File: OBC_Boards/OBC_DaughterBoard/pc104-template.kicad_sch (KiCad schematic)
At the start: 35 parts, among them J1 PC104_Connector, J2 ST11S008V4HR2000, U1 MCP79400T-I/SN, U2 MCP7940NT-I_MS, U3 BU33SA5WGWZ-E2-qsat-symb, Y1 CM9V-T1A

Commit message: working on pinout
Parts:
- removed G1: CR2032H, CR2032H:CR2032H, symbol CR2032H:CR2032H
- removed R?: 33, Daughterboard_footprints:RESC1608X55N, symbol Device:R
- removed R?: 10k, Daughterboard_footprints:RESC1608X55N, symbol Device:R
- added BT?: BVSD-2032-PC, Daughterboard_footprints:BAT_BVSD-2032-PC, symbol Daughterboard_Symbols:BVSD-2032-PC
- added C? (x2): 18pF, CAPC1608X90N, symbol Daughterboard_Symbols:CL10B104KB8NNNL
- added C? (x2): 10uF, CAPC1608X90N, symbol Daughterboard_Symbols:CL10B104KB8NNNL
- added C?: 0.1uF, CAPC1608X90N, symbol Daughterboard_Symbols:CL10B104KB8NNNL
- added FB? (x2): 100R @ 100 MHz, Daughterboard_footprints:BEADC1608X75N, symbol Device:FerriteBead_Small
- added J? (x3): Conn_01x04, Connector_PinHeader_2.54mm:PinHeader_1x04_P2.54mm_Vertical, symbol Connector_Generic:Conn_01x04
- added J?: Conn_02x06_Odd_Even, Connector_PinHeader_2.54mm:PinHeader_2x06_P2.54mm_Horizontal, symbol Connector_Generic:Conn_02x06_Odd_Even
- added R?: 33, Daughterboard_footprints:RESC1608X55N, symbol Device:R
- added R?: 20k, Daughterboard_footprints:RESC1608X55N, symbol Device:R
- added TP?: TestPoint, symbol Connector:TestPoint
- added U?: JS102011SCQN, Daughterboard_footprints:JS102011SCQN, symbol Daughterboard_Symbols:JS102011SCQN
- U3: footprint (none) -> STM32_Breakout:BU33SA5WGWZ-E2
- gave numbers to parts that had none: 17
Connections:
- net I2C_SCL is gone; now on net I2C_SCL1: U2.2 (X2)
- net I2C_SDA is gone; now on net I2C_SDA1: U2.1 (X1)
- net out is gone; now on net +3V3: MAX4372F1.6 (RS-), R1.2
- net +3.3V: now also C?.2
- net +3V3: now also J3.1 (Pin_1), J3.17 (Pin_17), FB?.1, FB?.2, TP?.1
- net GND: now also J1.81 (H2-29), J2.11 (GND1), J2.12 (GND2), J2.13 (GND3), J2.14 (GND4), J2.15 (GND5), J2.16 (GND6), J2.17 (GND7), J2.6 (VSS), J3.14 (Pin_14), J3.20 (Pin_20), J3.25 (Pin_25), J3.30 (Pin_30), J3.34 (Pin_34), J3.39 (Pin_39), J3.6 (Pin_6), J3.7 (Pin_7), J4.2 (Pin_2), J5.2 (Pin_2), C?.1, C?.1, C?.1, C?.2, C?.2, J?.2 (Pin_2), J?.2 (Pin_2), J?.2 (Pin_2), J?.3 (Pin_3), J?.4 (Pin_4)
- net GPIO_pin: now also R8.2, R?.2
- net PM_Input: now also J4.1 (Pin_1), MAX4372F1.8 (RS+), R1.1
- net at U1.1 (X1), Y1.1: now also C?.2
- net at U1.2 (X2), Y1.2: now also C?.2
- net UART_RXD0: now reaches J3.10 (Pin_10)
- net I2C_SDA6: now reaches J3.15 (Pin_15)
- net I2C_SCL6: now reaches J3.16 (Pin_16)
- net SPI1_MOSI: now reaches J3.19 (Pin_19)
- net SPI1_MOSI: now also J2.3 (CMD/DI)
- net 5V_Rpi_Input: now reaches J3.2 (Pin_2)
- net 5V_Rpi_Input: now also J3.4 (Pin_4), J5.1 (Pin_1), U4.2
- net SPI1_MISO: now reaches J3.21 (Pin_21)
- net SPI1_MISO: now also J2.7 (DAT0/DO)
- net SPI1_CLK: now reaches J3.23 (Pin_23)
- net SPI1_CLK: now also J2.5 (CLK)
- net SPI1_CE0_N: now reaches J3.24 (Pin_24)
- net SPI1_CE0_N: now also J2.2 (CS/DAT3)
- net SPI1_CE1_N: now reaches J3.26 (Pin_26)
- net I2C_SDA1: now reaches J3.3 (Pin_3)
- net I2C_SDA1: now also R4.2, U1.5 (SDA), J?.4 (Pin_4), J?.4 (Pin_4), J?.4 (Pin_4), J?.6 (Pin_6)
- net I2C_SDA5: now reaches J3.32 (Pin_32)
- net SPI_SCL5: now reaches J3.33 (Pin_33)
- net GPIO16: now reaches J3.36 (Pin_36)
- net GPIO16: now also J?.8 (Pin_8)
- net GPIO26: now reaches J3.37 (Pin_37)
- net GPIO26: now also J?.9 (Pin_9)
- net GPIO20: now reaches J3.38 (Pin_38)
- net GPIO20: now also J?.7 (Pin_7)
- net GPIO21: now reaches J3.40 (Pin_40)
- net GPIO21: now also J?.10 (Pin_10)
- net I2C_SCL1: now reaches J3.5 (Pin_5)
- net I2C_SCL1: now also R3.2, U1.6 (SCL), J?.3 (Pin_3), J?.3 (Pin_3), J?.3 (Pin_3), J?.5 (Pin_5)
- net UART_TXD0: now reaches J3.8 (Pin_8)
- net at J2.4 (VDD): now also R?.2
- net 5V_SInput: now reaches U4.3
- net 5V_SInput: now also U?.2
- net at C2.1, U3.2 (Output): now also R?.1; no longer R8.2
- net 5V_BInput: now reaches J1.77 (H2-25)
- net 5V_BInput: now also U?.3
- removed net +5V: MAX4372F1.1 (VCC), MAX4372F1.8 (RS+), R1.1
- net 5V_Input renamed 5V_VC_Input
- new net: R2.2, U1.7 (MFP)
- new net: FB?.1, MAX4372F1.1 (VCC)
- new net: C?.1, C?.1, FB?.2, R?.1
- new net 3V3_Input: J?.1 (Pin_1), J?.1 (Pin_1), J?.1 (Pin_1)
- new net 3V3_Output: J?.1 (Pin_1)
- new net 5V_CHG: J?.12 (Pin_12)
- new net 5V_DInput: J?.2 (Pin_2), U?.1
- new net GND_CHG: J?.11 (Pin_11)
- no-connect marks 106 -> 107
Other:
- moved on the sheet: J2, J3, J4, J5, U4

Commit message: Added MCP3008 to convert current monitor analog to serial for pi
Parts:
- added U5: MCP3008, MCP3008:Microchip-MCP3008-I_P-Manufacturer_Recommended, symbol Analog_ADC:MCP3008
- gave numbers to parts that had none: 16
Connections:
- net +3V3: now also MAX4372F1.5 (NC), U5.15 (Vref), U5.16 (Vdd)
- net GND: now also U5.14 (AGND), U5.9 (DGND); no longer MAX4372F1.3 (GND)
- net PM_Input: no longer MAX4372F1.8 (RS+), R1.1
- net SPI1_CLK: now also U5.13 (CLK)
- net SPI1_MISO: now also U5.12 (Dout)
- net SPI1_MOSI: now also U5.11 (Din)
- net at MAX4372F1.4 (OUT): now also U5.1 (CH0)
- new net: MAX4372F1.8 (RS+), R1.1
- new net GPIO_22?: U5.10 (~{CS}/SHDN)
- no-connect marks 107 -> 106
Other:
- note removed: "Current monitor"
- moved on the sheet: FB3, MAX4372F1, R1, TP1

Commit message: updates to schematic
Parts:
- removed J9: Conn_01x04, Connector_PinHeader_2.54mm:PinHeader_1x04_P2.54mm_Vertical, symbol Connector_Generic:Conn_01x04
- removed U4, U6: JS102011SCQN, Daughterboard_footprints:JS102011SCQN, symbol Daughterboard_Symbols:JS102011SCQN
- added D? (x2): RED, Daughterboard_footprints:CAPC1608X90N, symbol Simulation_SPICE:DIODE
- added FB? (x2): 100R @ 100 MHz, Daughterboard_footprints:BEADC1608X75N, symbol Device:FerriteBead_Small
- added J? (x2): Conn_01x04, Connector_PinHeader_2.54mm:PinHeader_1x04_P2.54mm_Vertical, symbol Connector_Generic:Conn_01x04
- added R? (x2): 2.2k, Daughterboard_footprints:RESC1608X55N, symbol Device:R
- added S1: EG1218, Daughterboard_footprints:EG1218, symbol Daughterboard_Symbols:EG1218
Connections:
- net 5V_CHG is gone; now on net BatVBUS: J6.12 (Pin_12)
- net 5V_DInput is gone; now on net 5V_Debug_Input: J6.2 (Pin_2)
- net 5V_VC_Input is gone; now on net 5V_Rpi_Input: FB1.2
- net GPIO_pin is gone; now on net Analog_Voltage: R7.2, R8.2
- net I2C_SCL6 is gone; now on net UART_RTS: J3.16 (Pin_16)
- net I2C_SDA6 is gone; now on net UART_CTS: J3.15 (Pin_15)
- net +3.3V: now also FB?.1; no longer C6.2, U1.8 (VCC)
- net +3V3: no longer J3.1 (Pin_1)
- net 3V3_Input: now also J?.1 (Pin_1), J?.1 (Pin_1)
- net 5V_Rpi_Input: now also S1.S
- net GND: now also J1.99 (H2-47), MAX4372F1.3 (GND), J?.2 (Pin_2), J?.2 (Pin_2), R?.2, R?.2; no longer J1.81 (H2-29)
- net I2C_SCL1: now also J1.10 (H1-10), J1.12 (H1-12), J1.14 (H1-14), J1.45 (H1-45), J1.6 (H1-6), J1.8 (H1-8)
- net I2C_SDA1: now also J1.11 (H1-11), J1.13 (H1-13), J1.44 (H1-44), J1.5 (H1-5), J1.7 (H1-7), J1.9 (H1-9)
- net UART_RXD0: now also J1.2 (H1-2)
- net UART_TXD0: now also J1.1 (H1-1)
- net GPIO6: now reaches J3.31 (Pin_31)
- net GPIO6: now also J?.3 (Pin_3)
- net GPIO19: now reaches J3.35 (Pin_35)
- net GPIO19: now also J?.4 (Pin_4)
- net at C7.1, C8.1, FB4.2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: now also D?.1 (A)
- net 3V3: now reaches MAX4372F1.8 (RS+), R1.1
- net 3V3: now also J3.1 (Pin_1), J4.1 (Pin_1), FB?.1
- net Analog_Voltage: now reaches U5.2 (CH1)
- net UART_CTS: now reaches J1.3 (H1-3)
- net UART_RTS: now reaches J1.4 (H1-4)
- net 5V_Debug_Input: now reaches J1.68 (H1-16)
- net 5V_Debug_Input: now also S1.P
- net BatVBUS: now reaches J1.97 (H2-45)
- net 5V_BInput: no longer names the net of J1.77 (H2-25)
- net GPIO_22? renamed SPI1_CEO_N
- net I2C_SDA5 renamed GPIO12
- net GPIO12: now also J?.4 (Pin_4)
- net PM_Input: no longer names the net of U3.4 (Vout)
- net PM_Input: now also FB?.2; no longer J4.1 (Pin_1)
- net SPI_SCL5 renamed GPIO13
- net GPIO13: now also J?.3 (Pin_3)
- new net: C6.2, D?.1 (A), FB?.2, U1.8 (VCC)
- new net: D?.2 (K), R?.1 (x2)
- no-connect marks 106 -> 88
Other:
- moved on the sheet: C6, J4, J5, J6, J7, J8, TP1

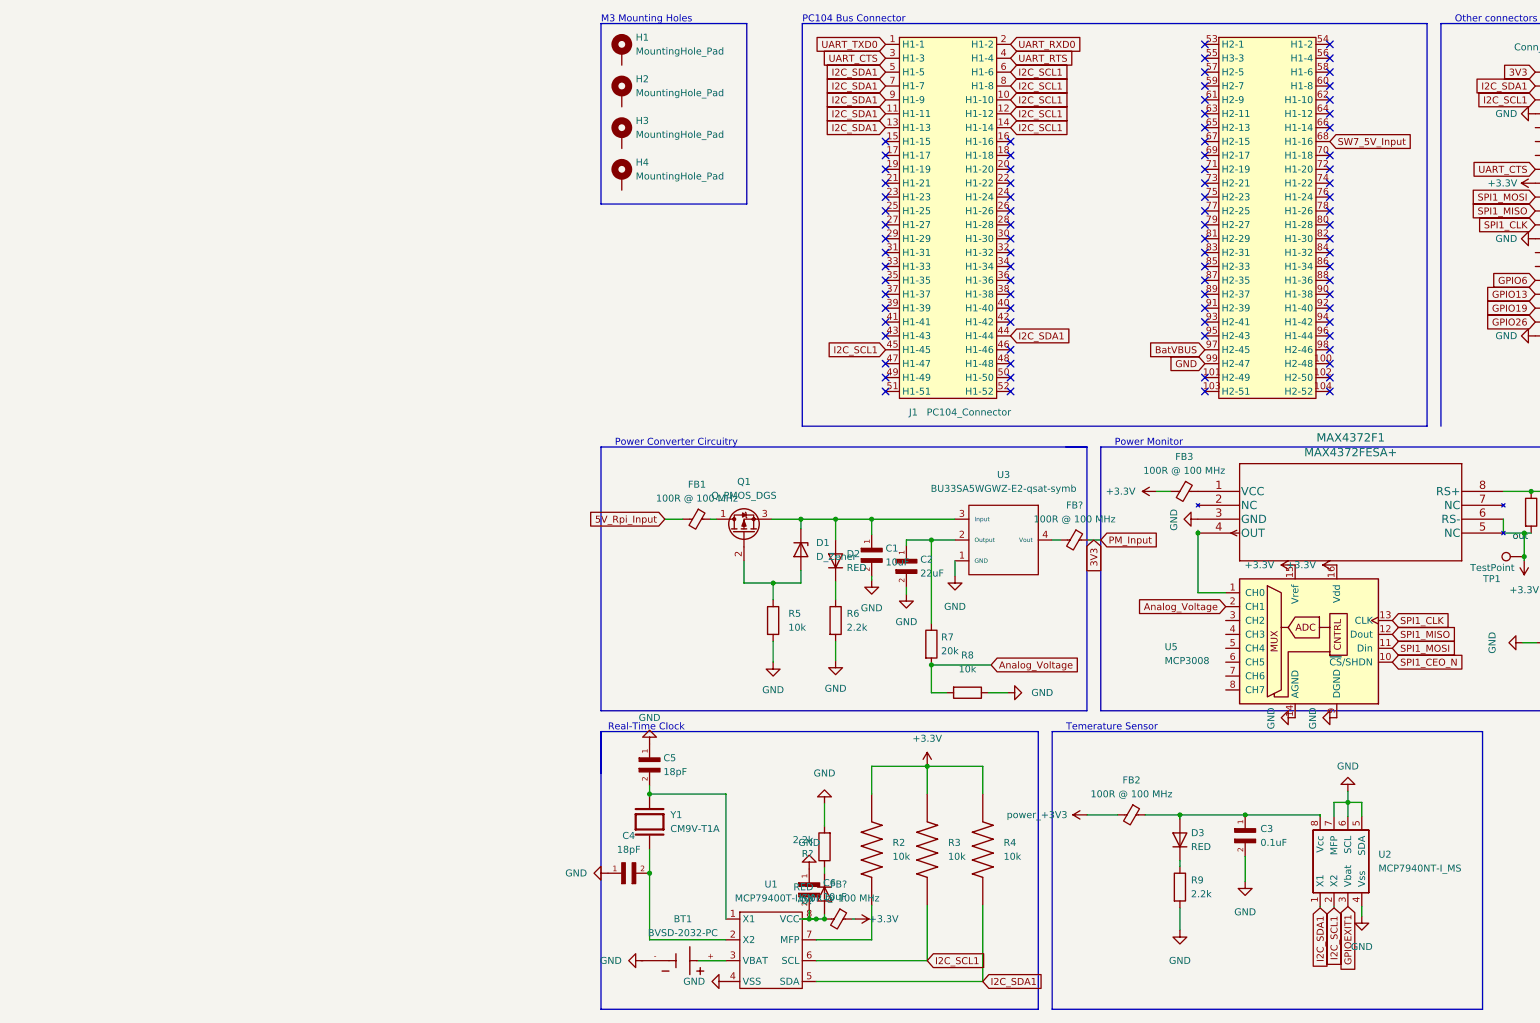
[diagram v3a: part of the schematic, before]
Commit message: obc: daughterboard: redo signal flags on pc104 bus connector
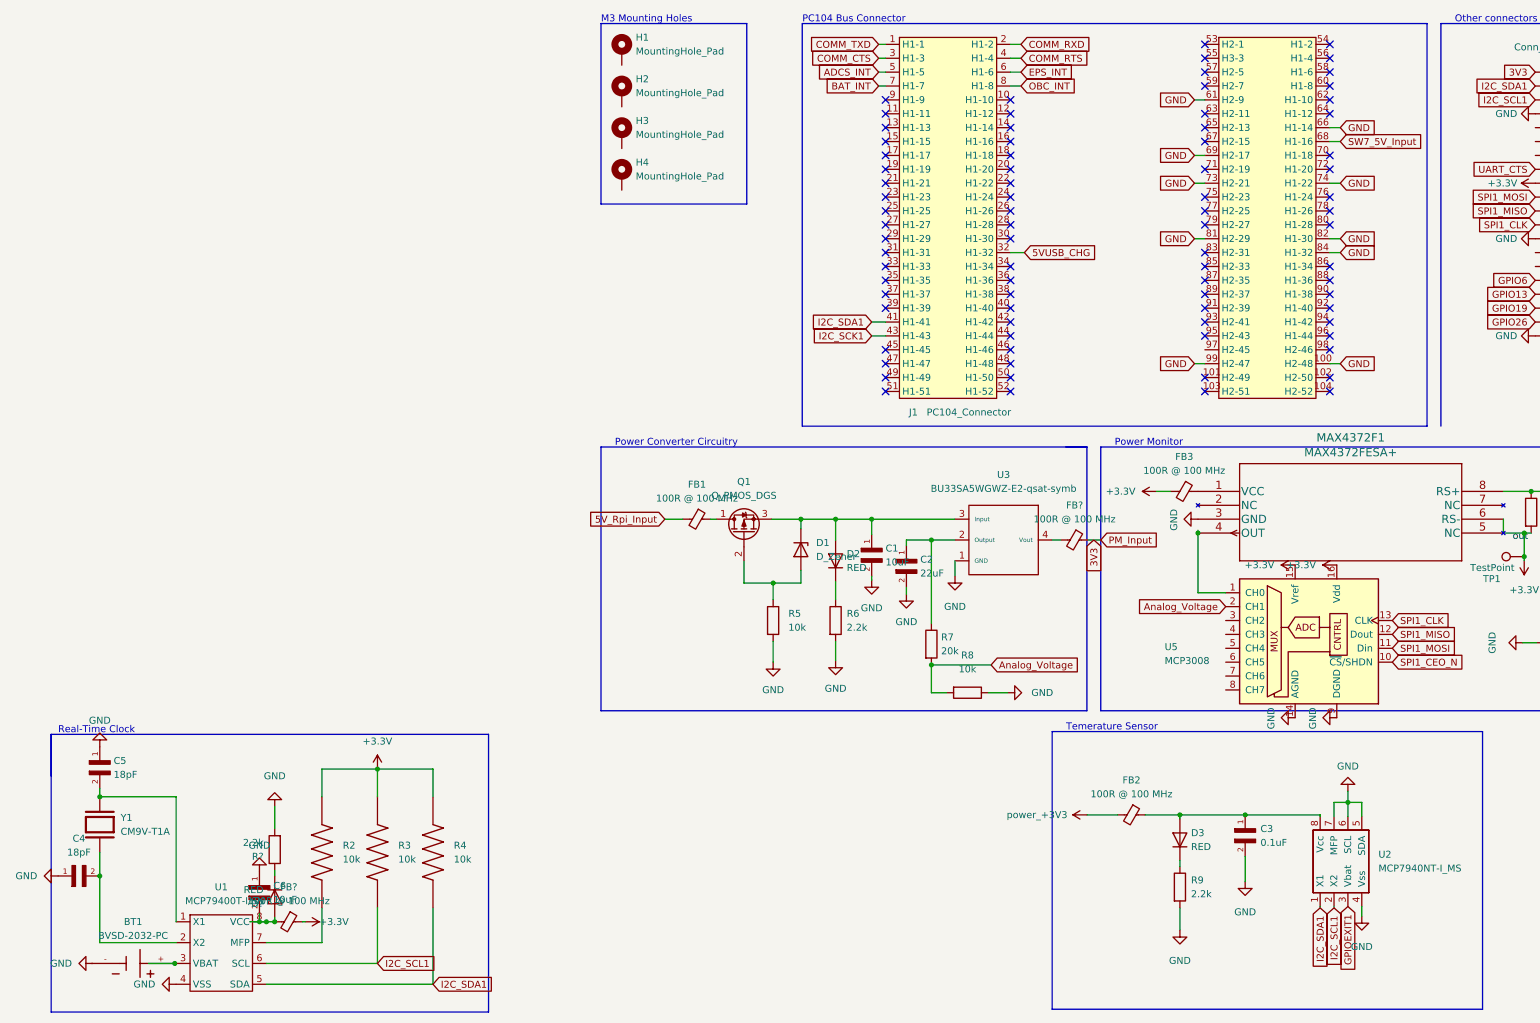
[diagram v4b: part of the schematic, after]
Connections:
- net BatVBUS: no longer J1.97 (H2-45)
- net GND: now also J1.100 (H2-48), J1.61 (H2-9), J1.66 (H1-14), J1.69 (H2-17), J1.73 (H2-21), J1.74 (H1-22), J1.81 (H2-29), J1.82 (H1-30), J1.84 (H1-32)
- net I2C_SCL1: no longer J1.10 (H1-10), J1.12 (H1-12), J1.14 (H1-14), J1.45 (H1-45), J1.6 (H1-6), J1.8 (H1-8)
- net I2C_SDA1: now also J1.41 (H1-41); no longer J1.11 (H1-11), J1.13 (H1-13), J1.44 (H1-44), J1.5 (H1-5), J1.7 (H1-7), J1.9 (H1-9)
- net UART_CTS: no longer J1.3 (H1-3)
- net UART_RTS: no longer J1.4 (H1-4)
- net UART_RXD0: no longer J1.2 (H1-2)
- net UART_TXD0: no longer J1.1 (H1-1)
- net at U1.3 (VBAT): now also BT1.+
- net 5VUSB_CHG: now reaches J1.32 (H1-32)
- net I2C_SCK1: now reaches J1.43 (H1-43)
- new net ADCS_INT: J1.5 (H1-5)
- new net BAT_INT: J1.7 (H1-7)
- new net COMM_CTS: J1.3 (H1-3)
- new net COMM_RTS: J1.4 (H1-4)
- new net COMM_RXD: J1.2 (H1-2)
- new net COMM_TXD: J1.1 (H1-1)
- new net EPS_INT: J1.6 (H1-6)
- new net OBC_INT: J1.8 (H1-8)
- no-connect marks 88 -> 84
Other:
- moved on the sheet: BT1, C4, C5, C6, D?, FB?, R2, R3, R4, R?, U1, Y1

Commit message: obc: daughterboard: clean up rtc section using hierarchical sheet
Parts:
- removed BT1: BVSD-2032-PC, Daughterboard_footprints:BAT_BVSD-2032-PC, symbol Daughterboard_Symbols:BVSD-2032-PC
- removed C4, C5: 18pF, CAPC1608X90N, symbol Daughterboard_Symbols:CL10B104KB8NNNL
- removed C6: 10uF, CAPC1608X90N, symbol Daughterboard_Symbols:CL10B104KB8NNNL
- removed D?: RED, Daughterboard_footprints:CAPC1608X90N, symbol Simulation_SPICE:DIODE
- removed FB?: 100R @ 100 MHz, Daughterboard_footprints:BEADC1608X75N, symbol Device:FerriteBead_Small
- removed R2, R3, R4: 10k, RESC1608X55N, symbol ESR03EZPF1002:ESR03EZPF1002
- removed R?: 2.2k, Daughterboard_footprints:RESC1608X55N, symbol Device:R
- removed U1: MCP79400T-I/SN, RTC Footprint:SOIC127P600X175-8N, symbol Timer_RTC:MCP79400T-I/SN
- removed Y1: CM9V-T1A, CM9V-T1A-32:XTAL_CM9V-T1A-32.768KHZ-9PF-20PPM-TA-QC, symbol CM9V-T1A-32.768KHZ-9PF-20PPM-TA-QC:CM9V-T1A-32.768KHZ-9PF-20PPM-TA-QC
- added R? (x3): 10k, RESC1608X55N, symbol ESR03EZPF1002:ESR03EZPF1002
- gave numbers to parts that had none: 5
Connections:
- net +3.3V: now also R?.1, R?.1, R?.1
- net I2C_SCK1: now also R?.2
- net I2C_SDA1: now also R?.2
- new net RTC_MFP: R?.2
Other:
- added sheet Real Time Clock (real-time-clock.kicad_sch)
- note added: "Pull Up Resistors"
- note removed: "Real-Time Clock"

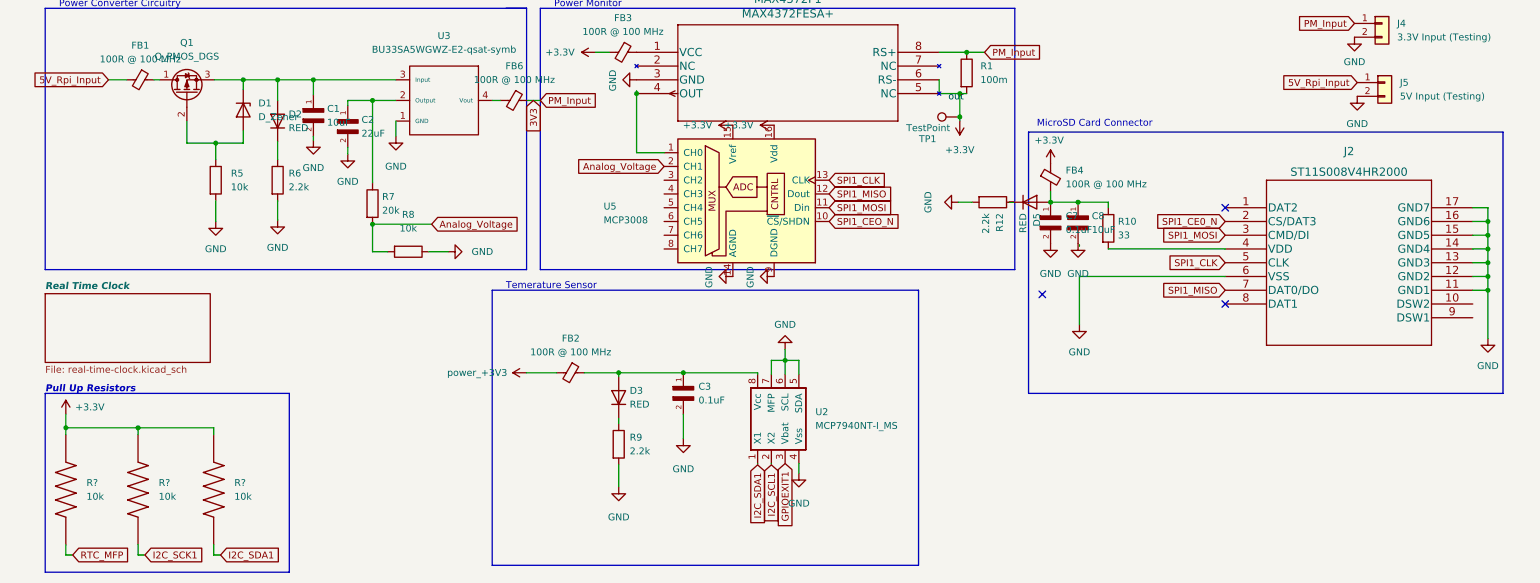
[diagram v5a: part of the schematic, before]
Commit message: obc: daughterboard: clean up microsd card section using hierarchical sheet
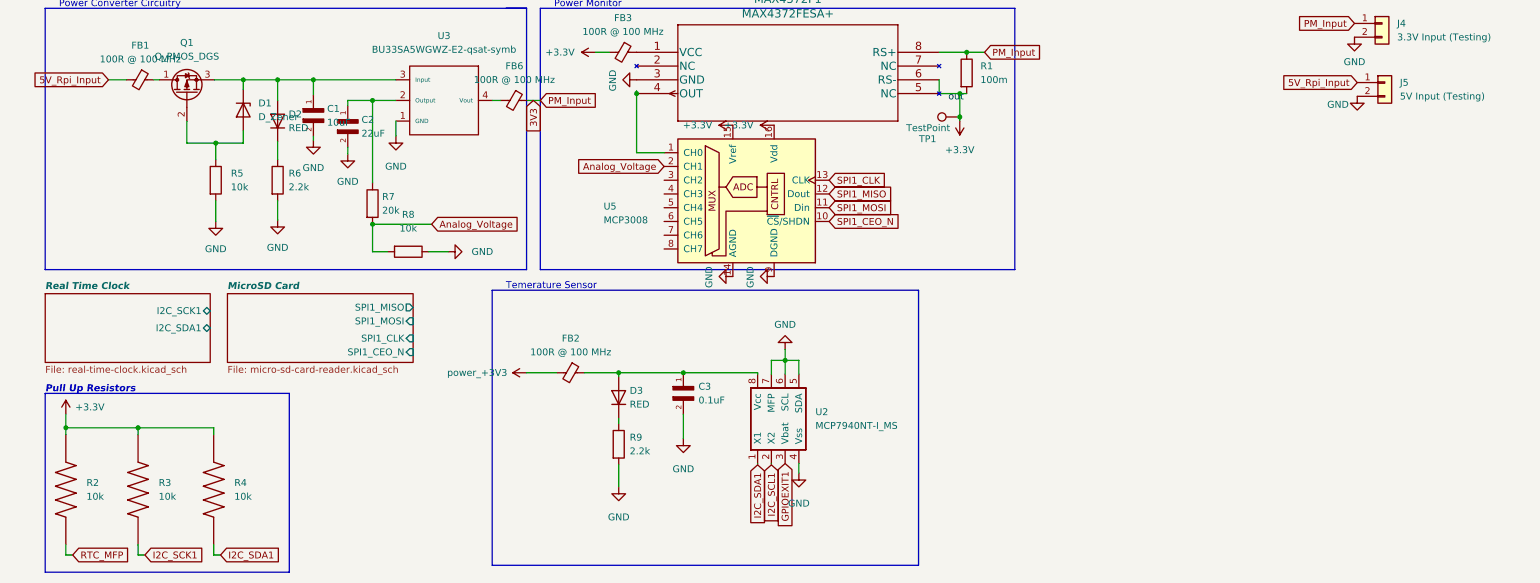
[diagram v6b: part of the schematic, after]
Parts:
- removed C7: 0.1uF, CAPC1608X90N, symbol Daughterboard_Symbols:CL10B104KB8NNNL
- removed C8: 10uF, CAPC1608X90N, symbol Daughterboard_Symbols:CL10B104KB8NNNL
- removed D5: RED, Daughterboard_footprints:CAPC1608X90N, symbol Simulation_SPICE:DIODE
- removed FB4: 100R @ 100 MHz, Daughterboard_footprints:BEADC1608X75N, symbol Device:FerriteBead_Small
- removed J2: ST11S008V4HR2000, STM32_Breakout:ST11S008V4HR2000, symbol Buffer:ST11S008V4HR2000
- removed R10: 33, Daughterboard_footprints:RESC1608X55N, symbol Device:R
- removed R12: 2.2k, Daughterboard_footprints:RESC1608X55N, symbol Device:R
- gave numbers to parts that had none: 3
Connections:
- no-connect marks 84 -> 81
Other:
- added sheet MicroSD Card (micro-sd-card-reader.kicad_sch)
- sheet Real Time Clock ports: added I2C_SCK1, I2C_SDA1; removed none
- note removed: "MicroSD Card Connector"
